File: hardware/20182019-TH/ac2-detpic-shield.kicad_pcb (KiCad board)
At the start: 2 copper layers, 99.1 x 69.6 mm, 54 parts, among them J1 HEADER, J2 HEADER, J3 HEADER, J4 HEADER, J5 HEADER, J6 HEADER, J7 HEADER, M1 M1, M2 M2, M3 MountingHole_2.2mm_M2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

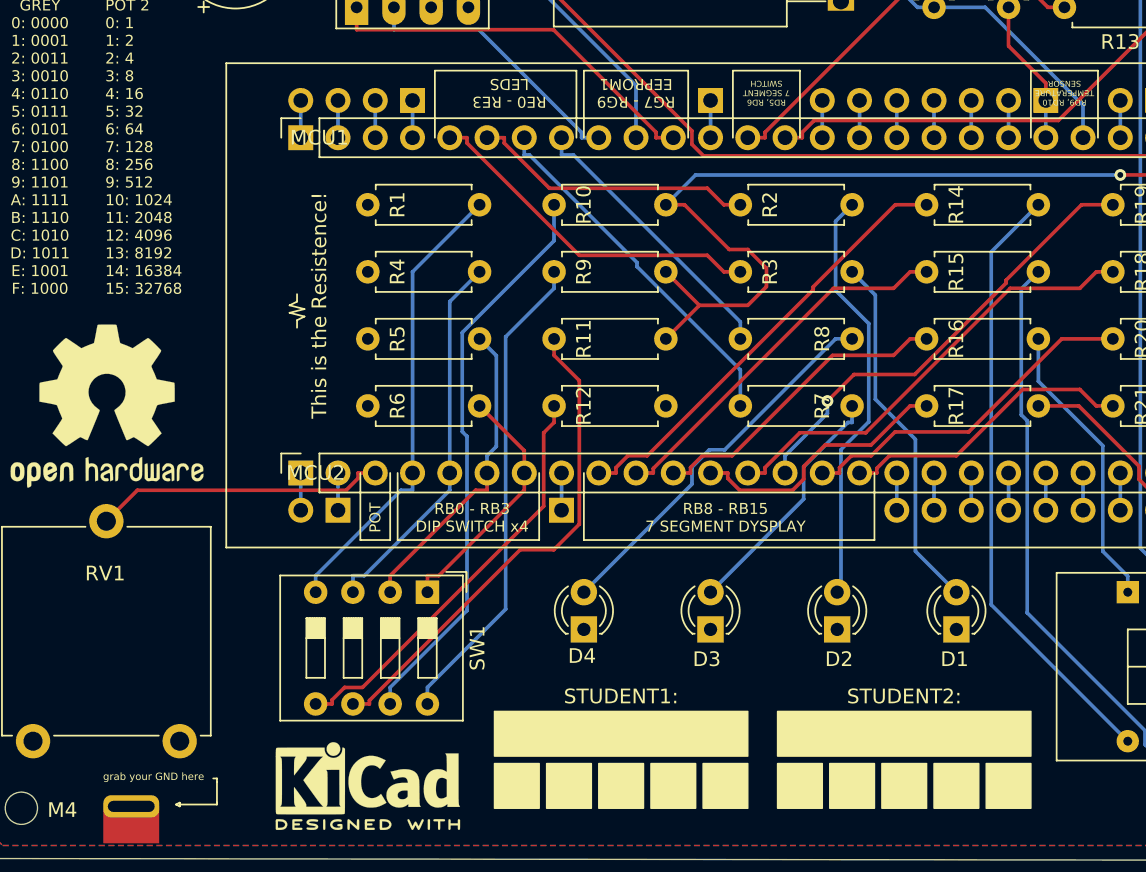
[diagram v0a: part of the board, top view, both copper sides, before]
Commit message: fixed bug in J3 header in 20182019-TH pcb
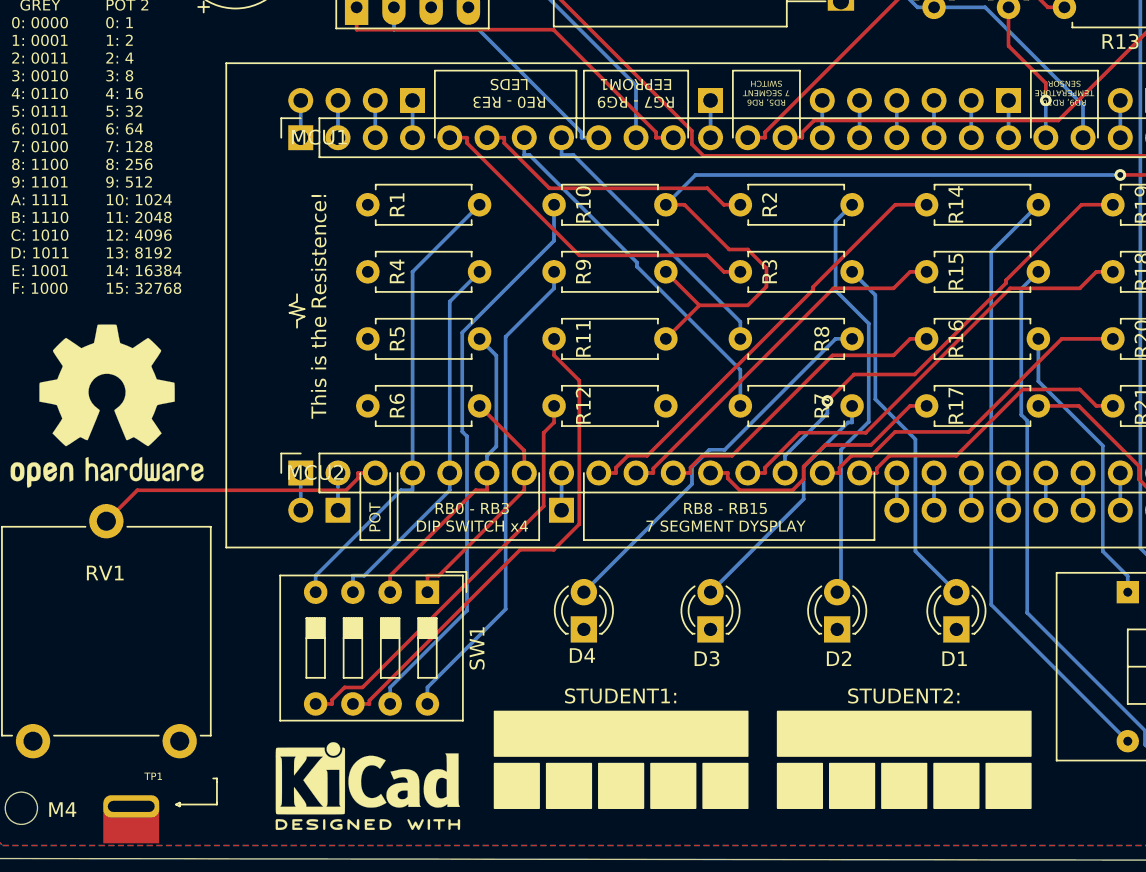
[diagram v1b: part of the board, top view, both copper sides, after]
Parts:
- J3: footprint Connector_PinHeader_2.54mm:PinHeader_1x07_P2.54mm_Vertical -> Connector_PinHeader_2.54mm:PinHeader_1x06_P2.54mm_Vertical
- TP1: renamed from grab your GND here
- moved J3 2.54 mm to (198.1, 43.2)
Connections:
- J3 pad 1: /RD10 -> /RD11
- J3 pad 2: /RD11 -> /RD0
- J3 pad 3: /RD0 -> /RD1
- J3 pad 4: /RD1 -> /RD2
- J3 pad 5: /RD2 -> /RD3
- J3 pad 6: /RD3 -> /RD4
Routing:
- net /RD10: vias 0 -> 1
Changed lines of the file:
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@@
     (thickness 1.6)
     (drawings 83)
-    (tracks 327)
+    (tracks 328)
     (zones 0)
     (modules 54)
@@
     (tags "test point SMD pad rectangle square")
     (attr virtual)
-    (fp_text reference "grab your GND here" (at 1.524 -3.302) (layer F.SilkS)
+    (fp_text reference TP1 (at 1.524 -3.302) (layer F.SilkS)
       (effects (font (size 0.5 0.5) (thickness 0.125)))
     )
@@
     )
   )
-  (module Connector_PinHeader_2.54mm:PinHeader_1x07_P2.54mm_Vertical (layer B.Cu)
-    (at 200.66 43.18 90)
-    (descr "Through hole straight pin header, 1x07, 2.54mm pitch, single row")
-    (tags "Through hole pin header THT 1x07 2.54mm single row")
+  (module Connector_PinHeader_2.54mm:PinHeader_1x06_P2.54mm_Vertical (layer B.Cu)
+    (at 198.12 43.18 90)
+    (descr "Through hole straight pin header, 1x06, 2.54mm pitch, single row")
+    (tags "Through hole pin header THT 1x06 2.54mm single row")
     (fp_text reference J3 (at 0 2.33 90) (layer B.SilkS)
       (effects (font (size 1 1) (thickness 0.15)) (justify mirror))
     )
-    (fp_text value HEADER (at 0 -17.57 90) (layer B.Fab)
+    (fp_text value HEADER (at 0 -15.03 90) (layer B.Fab)
       (effects (font (size 1 1) (thickness 0.15)) (justify mirror))
     )
     (fp_line (start -0.635 1.27) (end 1.27 1.27) (layer B.Fab) (width 0.1))
-    (fp_line (start 1.27 1.27) (end 1.27 -16.51) (layer B.Fab) (width 0.1))
-    (fp_line (start 1.27 -16.51) (end -1.27 -16.51) (layer B.Fab) (width 0.1))
-    (fp_line (start -1.27 -16.51) (end -1.27 0.635) (layer B.Fab) (width 0.1))
+    (fp_line (start 1.27 1.27) (end 1.27 -13.97) (layer B.Fab) (width 0.1))
+    (fp_line (start 1.27 -13.97) (end -1.27 -13.97) (layer B.Fab) (width 0.1))
+    (fp_line (start -1.27 -13.97) (end -1.27 0.635) (layer B.Fab) (width 0.1))
     (fp_line (start -1.27 0.635) (end -0.635 1.27) (layer B.Fab) (width 0.1))
-    (fp_line (start -1.33 -16.57) (end 1.33 -16.57) (layer B.SilkS) (width 0.12))
-    (fp_line (start -1.33 -1.27) (end -1.33 -16.57) (layer B.SilkS) (width 0.12))
-    (fp_line (start 1.33 -1.27) (end 1.33 -16.57) (layer B.SilkS) (width 0.12))
+    (fp_line (start -1.33 -14.03) (end 1.33 -14.03) (layer B.SilkS) (width 0.12))
+    (fp_line (start -1.33 -1.27) (end -1.33 -14.03) (layer B.SilkS) (width 0.12))
+    (fp_line (start 1.33 -1.27) (end 1.33 -14.03) (layer B.SilkS) (width 0.12))
     (fp_line (start -1.33 -1.27) (end 1.33 -1.27) (layer B.SilkS) (width 0.12))
     (fp_line (start -1.33 0) (end -1.33 1.33) (layer B.SilkS) (width 0.12))
     (fp_line (start -1.33 1.33) (end 0 1.33) (layer B.SilkS) (width 0.12))
-    (fp_line (start -1.8 1.8) (end -1.8 -17.05) (layer B.CrtYd) (width 0.05))
-    (fp_line (start -1.8 -17.05) (end 1.8 -17.05) (layer B.CrtYd) (width 0.05))
-    (fp_line (start 1.8 -17.05) (end 1.8 1.8) (layer B.CrtYd) (width 0.05))
+    (fp_line (start -1.8 1.8) (end -1.8 -14.5) (layer B.CrtYd) (width 0.05))
+    (fp_line (start -1.8 -14.5) (end 1.8 -14.5) (layer B.CrtYd) (width 0.05))
+    (fp_line (start 1.8 -14.5) (end 1.8 1.8) (layer B.CrtYd) (width 0.05))
     (fp_line (start 1.8 1.8) (end -1.8 1.8) (layer B.CrtYd) (width 0.05))
-    (fp_text user %R (at 0 -7.62) (layer B.Fab)
+    (fp_text user %R (at 0 -6.35) (layer B.Fab)
       (effects (font (size 1 1) (thickness 0.15)) (justify mirror))
     )
     (pad 1 thru_hole rect (at 0 0 90) (size 1.7 1.7) (drill 1) (layers *.Cu *.Mask)
-      (net 27 /RD10))
-    (pad 2 thru_hole oval (at 0 -2.54 90) (size 1.7 1.7) (drill 1) (layers *.Cu *.Mask)
       (net 26 /RD11))
-    (pad 3 thru_hole oval (at 0 -5.08 90) (size 1.7 1.7) (drill 1) (layers *.Cu *.Mask)
+    (pad 2 thru_hole oval (at 0 -2.54 90) (size 1.7 1.7) (drill 1) (layers *.Cu *.Mask)
       (net 25 /RD0))
-    (pad 4 thru_hole oval (at 0 -7.62 90) (size 1.7 1.7) (drill 1) (layers *.Cu *.Mask)
+    (pad 3 thru_hole oval (at 0 -5.08 90) (size 1.7 1.7) (drill 1) (layers *.Cu *.Mask)
       (net 24 /RD1))
-    (pad 5 thru_hole oval (at 0 -10.16 90) (size 1.7 1.7) (drill 1) (layers *.Cu *.Mask)
+    (pad 4 thru_hole oval (at 0 -7.62 90) (size 1.7 1.7) (drill 1) (layers *.Cu *.Mask)
       (net 23 /RD2))
-    (pad 6 thru_hole oval (at 0 -12.7 90) (size 1.7 1.7) (drill 1) (layers *.Cu *.Mask)
+    (pad 5 thru_hole oval (at 0 -10.16 90) (size 1.7 1.7) (drill 1) (layers *.Cu *.Mask)
       (net 22 /RD3))
-    (pad 7 thru_hole oval (at 0 -15.24 90) (size 1.7 1.7) (drill 1) (layers *.Cu *.Mask)
+    (pad 6 thru_hole oval (at 0 -12.7 90) (size 1.7 1.7) (drill 1) (layers *.Cu *.Mask)
       (net 21 /RD4))
-    (model ${KISYS3DMOD}/Connector_PinHeader_2.54mm.3dshapes/PinHeader_1x07_P2.54mm_Vertical.wrl
+    (model ${KISYS3DMOD}/Connector_PinHeader_2.54mm.3dshapes/PinHeader_1x06_P2.54mm_Vertical.wrl
       (at (xyz 0 0 0))
       (scale (xyz 1 1 1))
@@
   (segment (start 186.69 31.32) (end 192.61 31.32) (width 0.25) (layer B.Cu) (net 27))
   (segment (start 192.61 31.32) (end 198.12 36.83) (width 0.25) (layer B.Cu) (net 27))
+  (via (at 200.66 43.18) (size 0.8) (drill 0.4) (layers F.Cu B.Cu) (net 27))
   (segment (start 200.66 43.18) (end 200.66 45.72) (width 0.25) (layer B.Cu) (net 27))
   (segment (start 193.04 36.83) (end 191.9147 36.83) (width 0.25) (layer B.Cu) (net 28))

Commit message: new gerbers and fix in README.md of the 20192018-TH board
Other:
- board text added: "grab your GND here"
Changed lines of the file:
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@@
   (general
     (thickness 1.6)
-    (drawings 83)
+    (drawings 84)
     (tracks 328)
     (zones 0)
@@
     (tags "test point SMD pad rectangle square")
     (attr virtual)
-    (fp_text reference TP1 (at 1.524 -3.302) (layer F.SilkS)
+    (fp_text reference TP1 (at 2.921 -0.127) (layer F.SilkS)
       (effects (font (size 0.5 0.5) (thickness 0.125)))
     )
@@
     )
   )
+  (gr_text "grab your GND here" (at 139.7 89.408) (layer F.SilkS)
+    (effects (font (size 0.5 0.5) (thickness 0.125)))
+  )
   (gr_line (start 144.145 89.408) (end 143.891 89.408) (layer F.SilkS) (width 0.12))

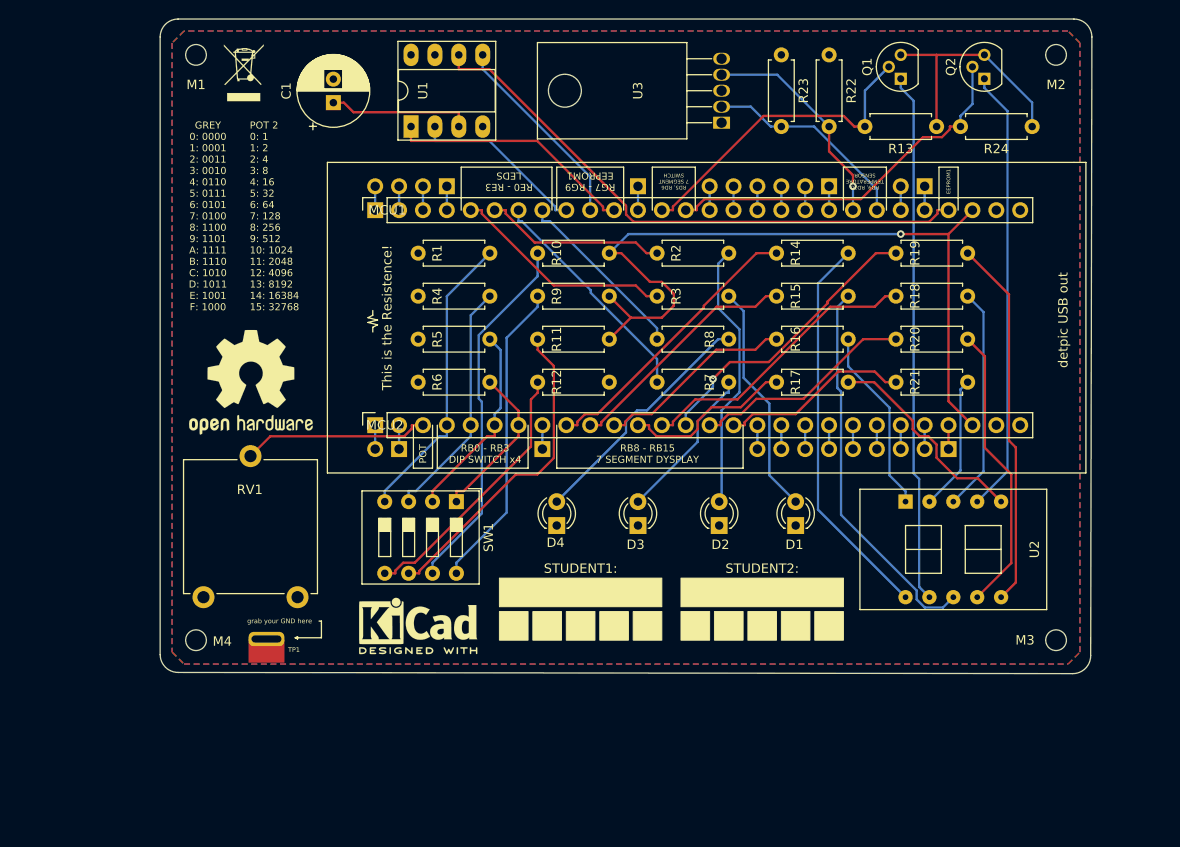
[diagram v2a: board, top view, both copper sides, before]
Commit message: rotary pot, option on dual single 7seg displays and fix in trim pot
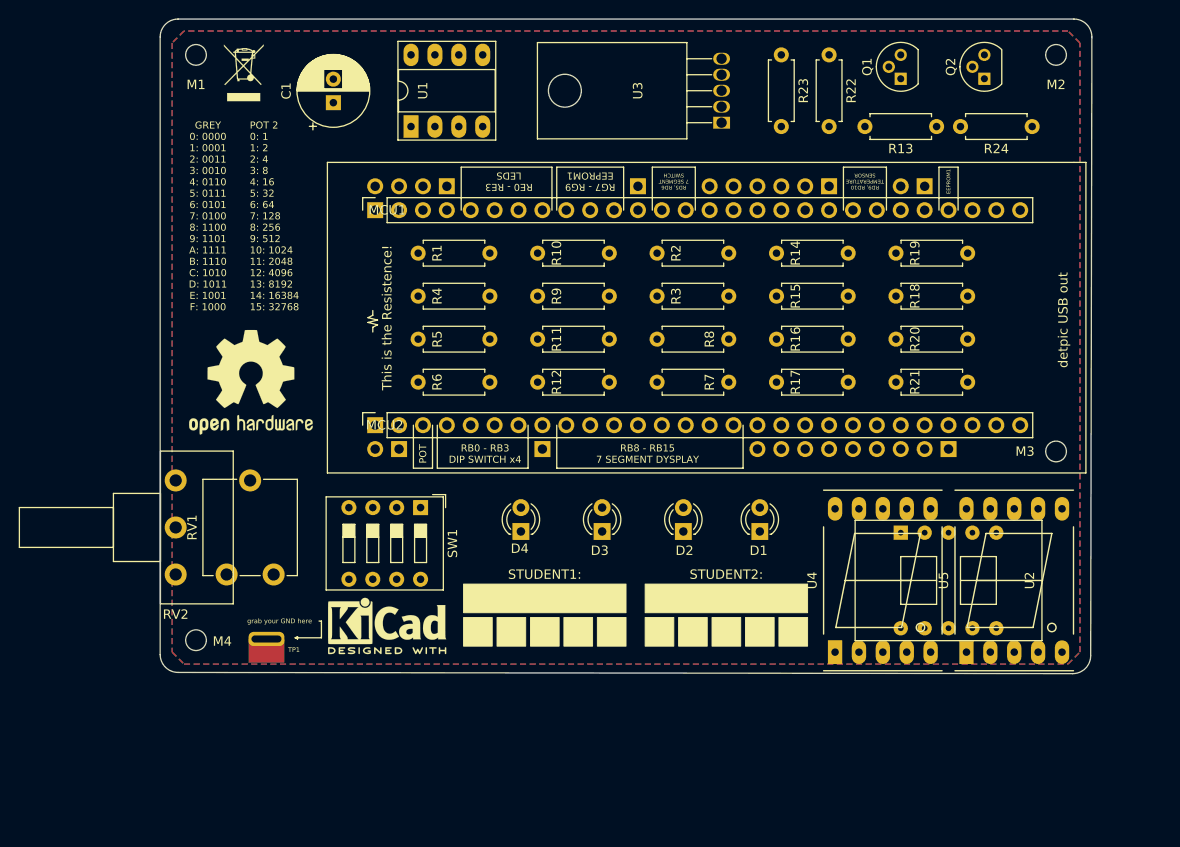
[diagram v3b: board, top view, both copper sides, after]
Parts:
- added RV2: 10k, Potentiometer_THT:Potentiometer_Piher_T-16H_Single_Horizontal, F.Cu at (128.7, 74.5)
- added U4: KCSA02-107, Display_7Segment:7SegmentLED_LTS6760_LTS6780, F.Cu at (198.8, 92.7)
- added U5: KCSA02-107, Display_7Segment:7SegmentLED_LTS6760_LTS6780, F.Cu at (212.7, 92.7)
- RV1: footprint Potentiometer_THT:Potentiometer_ACP_CA14V-15_Vertical -> Potentiometer_THT:Potentiometer_ACP_CA9-V10_Vertical
- moved M3 20.1 mm to (222.2, 71.4)
- moved SW1 3.86 mm to (154.7, 77.3)
- moved D1 3.86 mm to (190.8, 79.9)
- moved D2 3.86 mm to (182.6, 79.9)
- moved D3 3.86 mm to (174.0, 79.9)
- moved D4 3.86 mm to (165.4, 79.9)
- moved RV1 3.50 mm to (139.1, 84.5)
- moved U2 3.34 mm to (210.8, 85.1)
- moved REF3 3.30 mm to (151.1, 89.9)
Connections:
- net Net-(Q1-Pad1) renamed /7C1
- net Net-(Q2-Pad1) renamed /7C2
- net Net-(R14-Pad1) renamed /7A
- net Net-(R15-Pad1) renamed /7B
- net Net-(R16-Pad1) renamed /7C
- net Net-(R17-Pad1) renamed /7D
- net Net-(R18-Pad1) renamed /7E
- net Net-(R19-Pad1) renamed /7F
- net Net-(R20-Pad1) renamed /7G
- net Net-(R21-Pad1) renamed /7DP
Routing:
- net /+3.3V: track 83.4 -> 0.00 mm, vias 1 -> 0
- net /RG6: track 61.6 -> 0.00 mm
- net /7C1: track 56.4 -> 0.00 mm
- net /7C2: track 47.3 -> 0.00 mm
- net /7A: track 41.8 -> 0.00 mm
- net /7B: track 40.9 -> 0.00 mm
- net /RD5: track 40.1 -> 0.00 mm
- net /7F: track 39.3 -> 0.00 mm
- net Net-(R10-Pad2): track 38.9 -> 0.00 mm
- net Net-(R11-Pad2): track 34.0 -> 0.00 mm
- net /RD6: track 33.8 -> 0.00 mm
- net Net-(R9-Pad2): track 33.0 -> 0.00 mm
- net /RB3: track 31.5 -> 0.00 mm
- net /RB13: track 31.2 -> 0.00 mm, vias 1 -> 0
- net /7G: track 30.9 -> 0.00 mm
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
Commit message: changes docs of detpic to common directory + changes in the pcb and footprint (rotary pot)
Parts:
- RV2: footprint Potentiometer_THT:Potentiometer_Piher_T-16H_Single_Horizontal -> Potentiometer_THT:Potentiometer_Alps_RK163_Single_Horizontal
- moved RV2 2.41 mm to (131.1, 74.5)
- moved R18 2.03 mm to (214.9, 54.9)
- moved R19 2.03 mm to (214.9, 50.3)
- moved R20 2.03 mm to (214.9, 59.4)
- moved R21 2.03 mm to (214.9, 64.0)
- moved R14 1.52 mm to (201.7, 50.3)
- moved R15 1.52 mm to (201.7, 54.9)
- moved R16 1.52 mm to (201.7, 59.4)
- moved R17 1.52 mm to (201.7, 64.0)
- moved R7 1.02 mm to (180.8, 64.0)
- moved R8 1.02 mm to (180.8, 59.4)
- moved R2 1.02 mm to (188.5, 50.3)
- moved R3 1.02 mm to (188.5, 54.9)
- moved R10 0.51 mm to (175.3, 50.3)
- moved R11 0.51 mm to (175.3, 59.4)
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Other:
- board text added: "This is the Resistance!"
- board text removed: "This is the Resistence!"
